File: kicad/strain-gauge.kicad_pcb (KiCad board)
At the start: 2 copper layers, 16.2 x 28 mm, 17 parts, among them J1 Left, J2 Right, U1 ADS8691IPWR, U2 TMUX131RMG, U3 SN74HCS72QDRQ1, U4 74AHC1G00, U5 AD8421

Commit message: small fixes
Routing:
- net GND: track 28.8 -> 29.4 mm, vias 12 -> 15
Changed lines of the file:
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@@
 			(outputformat 1)
 			(mirror no)
-			(drillshape 1)
+			(drillshape 0)
 			(scaleselection 1)
-			(outputdirectory "")
+			(outputdirectory "gerbers/")
 		)
 	)
@@
 	)
 	(segment
+		(start 95.06 123.52415)
+		(end 94.72585 123.52415)
+		(width 0.2)
+		(layer "F.Cu")
+		(net 1)
+	)
+	(segment
 		(start 86.475 135.55)
 		(end 85.3 135.55)
@@
 	)
 	(segment
+		(start 94.72585 123.52415)
+		(end 94.5 123.75)
+		(width 0.2)
+		(layer "F.Cu")
+		(net 1)
+	)
+	(segment
 		(start 98.5 123.75)
 		(end 97 123.75)
@@
 	)
 	(via
+		(at 98.75 115.25)
+		(size 0.6)
+		(drill 0.3)
+		(layers "F.Cu" "B.Cu")
+		(free yes)
+		(net 1)
+	)
+	(via
 		(at 85.05 139)
 		(size 0.6)
@@
 	)
 	(via
+		(at 94 118.75)
+		(size 0.6)
+		(drill 0.3)
+		(layers "F.Cu" "B.Cu")
+		(free yes)
+		(net 1)
+	)
+	(via
 		(at 89.75 128.75)
 		(size 0.6)
@@
 	)
 	(via
+		(at 98.25 122.25)
+		(size 0.6)
+		(drill 0.3)
+		(layers "F.Cu" "B.Cu")
+		(free yes)
+		(net 1)
+	)
+	(via
 		(at 96.75 127.75)
 		(size 0.6)
@@
 	)
 	(via
-		(at 95.06 123.5)
+		(at 94.5 123.75)
 		(size 0.6)
 		(drill 0.3)
@@
 		(min_thickness 0.25)
 		(filled_areas_thickness no)
-		(fill
+		(fill yes
 			(thermal_gap 0.5)
 			(thermal_bridge_width 0.5)

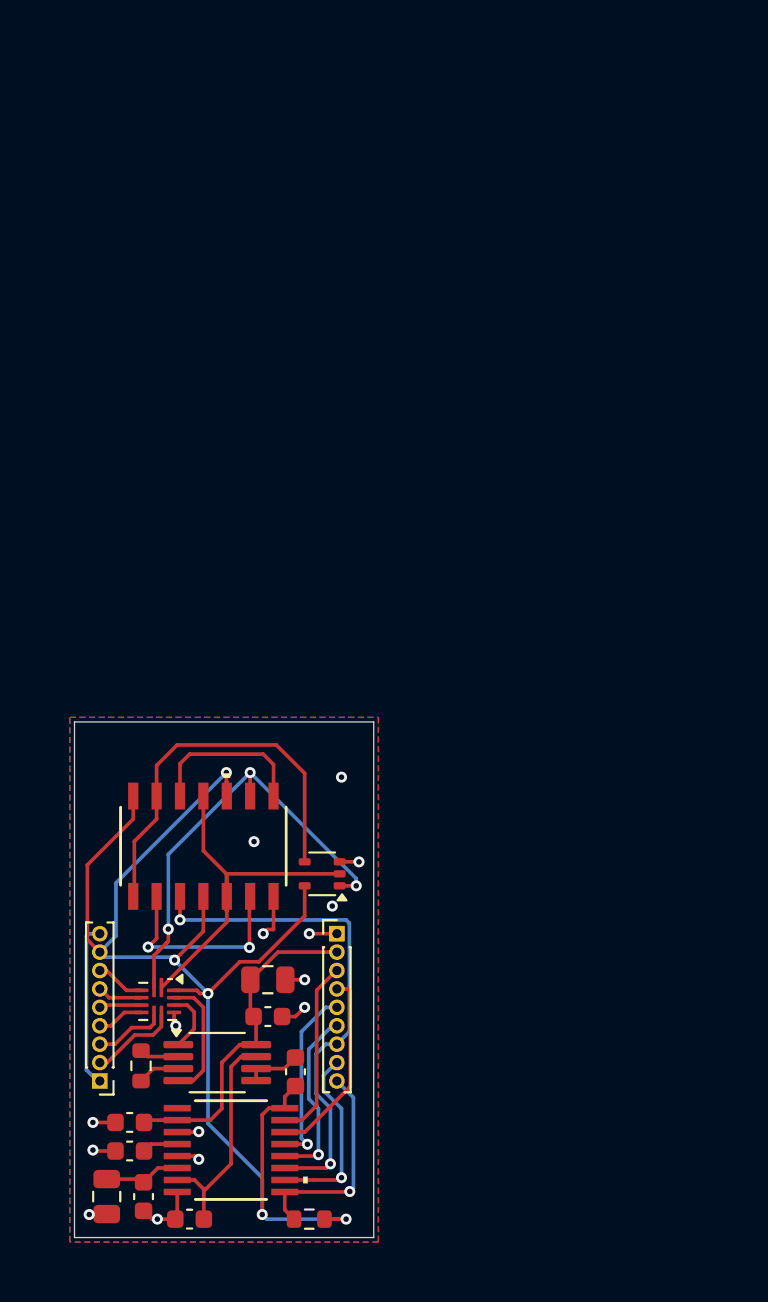
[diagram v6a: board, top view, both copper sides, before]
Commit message: redo routing with correct header pin footprint
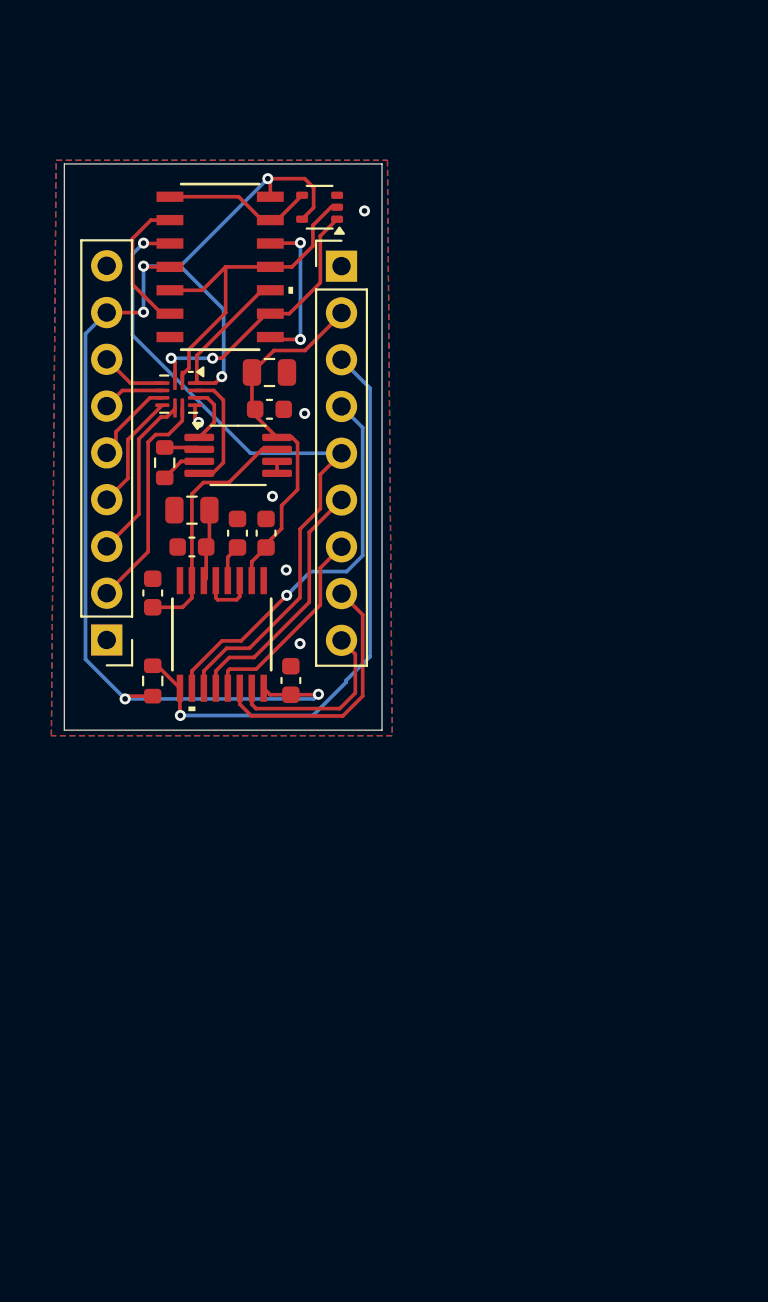
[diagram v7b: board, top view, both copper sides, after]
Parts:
- J1, J2: footprint Connector_PinHeader_1.00mm:PinHeader_1x09_P1.00mm_Vertical -> Connector_PinHeader_2.54mm:PinHeader_1x09_P2.54mm_Vertical
- moved C1 37.6 mm to (90.6, 100.8), turned to 0 degrees
- moved J2 36.3 mm to (98.8, 87.5)
- moved U4 36.2 mm to (97.6, 84.3)
- moved C2 35.4 mm to (90.6, 102.8), turned to 0 degrees
- moved C5 34.1 mm to (88.5, 105.2), turned to 90 degrees
- moved C3 34.1 mm to (93.1, 102.0), turned to 90 degrees
- moved U2 33.0 mm to (89.9, 94.5)
- moved U5 33.0 mm to (93.1, 97.8)
- moved C7 33.0 mm to (94.8, 95.3)
- moved C8 33.0 mm to (94.8, 93.3)
- moved C4 32.8 mm to (94.7, 102.0), turned to 90 degrees
- moved R1 32.8 mm to (89.1, 98.2)
- moved U3 31.5 mm to (92.2, 87.5), turned to 0 degrees
- moved R2 30.4 mm to (88.5, 110.0), turned to -90 degrees
- moved U1 28.0 mm to (92.2, 107.5), turned to -90 degrees
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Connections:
- J2 pad 3: /ADC/RVS -> /ADC/~{RST}
- J2 pad 4: /ADC/SDO-1 -> /ADC/SDI
- J2 pad 5: /ADC/SDO-0 -> /ADC/~{CS}
- J2 pad 7: /ADC/~{CS} -> /ADC/SDO-0
- J2 pad 8: /ADC/SDI -> /ADC/SDO-1
- J2 pad 9: /ADC/~{RST} -> /ADC/RVS
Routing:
- net GND: track 29.4 -> 4.88 mm, vias 15 -> 6
- net /ADC/~{RST}: track 11.7 -> 31.9 mm
- net Net-(U3-~{1CLR}): track 21.6 -> 8.26 mm
- net /ADC/SDI: track 10.1 -> 21.4 mm
- net /ADC/~{CS}: track 27.6 -> 37.3 mm, vias 2 -> 1
- net /Counter/SEL1: track 24.6 -> 14.9 mm, vias 3 -> 2
- net /Multiplexer/A_IN_N1: track 4.78 -> 12.2 mm
- net /Multiplexer/A_IN_P1: track 3.86 -> 9.28 mm
- net /ADC/SCLK: track 9.86 -> 13.8 mm, vias 1 -> 0
- net /Multiplexer/A_IN_N3: track 2.56 -> 6.38 mm
- net /ADC/SDO-1: track 10.5 -> 14.3 mm
- net Net-(U3-1D): track 11.2 -> 7.64 mm, vias 2 -> 0
- net /Multiplexer/A_IN_P3: track 2.49 -> 4.63 mm
- net /Counter/SEL0: track 20.5 -> 18.7 mm
- net +5V: track 18.3 -> 20.1 mm
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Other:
- board size 16.2 x 28 mm -> 17.2 x 30.8 mm
